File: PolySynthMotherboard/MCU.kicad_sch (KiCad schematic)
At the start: 21 parts, among them U201 STM32F411RETx, U202 74HC595, U203 74HC595, Y201 16MHz, Y202 32.768kHZ

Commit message: power supply/ output circuits
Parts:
- added C216, C217: 100n, Capacitor_SMD:C_0805_2012Metric, symbol Device:C
- added D201: 1N4148, Diode_THT:D_DO-35_SOD27_P7.62mm_Horizontal, symbol Diode:1N4148
- added D503: PMEG3030, PCM_Diode_SMD_AKL:D_SOD-123, symbol Device:D_Schottky
- added J201: SWD Header, Connector_PinHeader_1.27mm:PinHeader_2x07_P1.27mm_Horizontal, symbol Connector:ST_SWDHeader_3Wire
- added J202: USB_C_Receptacle_USB2.0, Connector_USB:USB_C_Receptacle_JAE_DX07S016JA1R1500, symbol Connector:USB_C_Receptacle_USB2.0
- added J203: MIDI_In, Connector_PinSocket_2.54mm:PinSocket_1x02_P2.54mm_Vertical, symbol Connector:Conn_01x02_Pin
- added J204: MIDI_Thru, Connector_PinSocket_2.54mm:PinSocket_1x02_P2.54mm_Vertical, symbol Connector:Conn_01x02_Pin
- added J205: MIDI_Out, Connector_PinSocket_2.54mm:PinSocket_1x02_P2.54mm_Vertical, symbol Connector:Conn_01x02_Pin
- added J401: Micro_SD_Card_Det2, Connector_Card:microSD_HC_Hirose_DM3D-SF, symbol Connector:Micro_SD_Card_Det2
- added R201, R202: 100k, PCM_Resistor_SMD_AKL:R_0805_2012Metric, symbol Device:R_US
- added R203: 4k7, PCM_Resistor_SMD_AKL:R_0805_2012Metric, symbol Device:R_US
- added R204, R206, R207, R208, R209: 220, PCM_Resistor_SMD_AKL:R_0805_2012Metric, symbol Device:R_US
- added R205: 470, PCM_Resistor_SMD_AKL:R_0805_2012Metric, symbol Device:R_US
- added R404: 47k, PCM_Resistor_SMD_AKL:R_0805_2012Metric, symbol Device:R_US
- added SW201: RST, Button_Switch_SMD:SW_SPST_B3U-1000P, symbol Switch:SW_SPST
- added SW202: BOOT, Button_Switch_SMD:SW_SPST_B3U-1000P, symbol Switch:SW_SPST
- added U204: 4N35, Package_DIP:DIP-6_W7.62mm, symbol Isolator:4N35
- added U205: 74HC04, PCM_Package_SO_AKL:SOIC-14_3.9x8.7mm_P1.27mm, symbol 74xx:74HC04
- C201, C202, C203, C204, C205, C208, C209, C210, C214, C215: footprint (none) -> Capacitor_SMD:C_0805_2012Metric
- U202, U203: footprint (none) -> Package_SO:SOIC-16_3.9x9.9mm_P1.27mm
- Y202: footprint (none) -> Crystal:Crystal_SMD_SeikoEpson_MC306-4Pin_8.0x3.2mm
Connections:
- net +3.3V: now also C217.1, J201.2 (VCC), J401.4 (VDD), R201.1, R205.1, R207.1, R209.1, R404.1, SW202.2 (B), U205.14 (VCC)
- net BOOT0: now also R202.1, SW202.1 (A)
- net DAC_A0: now also U201.27 (PB1); no longer U201.42 (PA9)
- net DAC_A1: now also U201.28 (PB2); no longer U201.43 (PA10)
- net DAC_A2: now also U201.29 (PB10); no longer U201.44 (PA11)
- net EXP_CS: now also U201.33 (PB12); no longer U201.50 (PA15)
- net EXP_MISO: now also U201.35 (PB14); no longer U201.52 (PC11)
- net EXP_MOSI: now also U201.36 (PB15); no longer U201.53 (PC12)
- net EXP_SCK: now also U201.34 (PB13); no longer U201.51 (PC10)
- net GND: now also C216.2, C217.2, J201.1 (GND), J202.A1 (GND), J202.A12 (GND), J202.B1 (GND), J202.B12 (GND), J202.S1 (SHIELD), J401.11 (SHIELD), J401.6 (VSS), R202.2, R203.2, SW201.1 (A), U204.4, U205.7 (GND)
- net NRST: now also C216.1, J201.6 (RST), R201.2, SW201.2 (B)
- net PITCH_MOSI: now also U201.23 (PA7)
- net PITCH_SCK: now also U201.21 (PA5)
- net POTS_SCL: now also U201.61 (PB8); no longer U201.58 (PB6)
- net POTS_SDA: now also U201.62 (PB9); no longer U201.59 (PB7)
- net SWO: now also J201.5 (SWO)
- net TCK: now also J201.3 (SWCLK)
- net TMS: now also J201.4 (SWDIO)
- net PIXELS_MAIN: now reaches U201.15 (PA1)
- net EXP_INTR_A: now reaches U201.37 (PC6)
- net EXP_INTR_B: now reaches U201.38 (PC7)
- net USB_D+: now reaches U201.45 (PA12)
- net USB_D+: now also J202.A6 (D+), J202.B6 (D+)
- net SD_CS: now reaches U201.54 (PD2)
- net SD_CS: now also J401.2 (DAT3/CD), R404.2
- net DISP_DC: now reaches U201.56 (PB4)
- net DISP_RST: now reaches U201.57 (PB5)
- net BATT_REF: now reaches U201.9 (PC1)
- net USART_RX: no longer names the net of U201.17 (PA3)
- net USART_TX renamed PIXELS_MATRIX
- new net: J204.2 (Pin_2), R207.2
- new net: D201.1 (K), J203.2 (Pin_2), U204.1
- new net: D201.2 (A), R204.1, U204.2
- new net: J202.A5 (CC1), J202.B5 (CC2), R203.1
- new net: U205.2, U205.3
- new net: R206.2, U205.4
- new net: J204.1 (Pin_1), R206.1
- new net: J205.2 (Pin_2), R209.2
- new net: J203.1 (Pin_1), R204.2
- new net: J205.1 (Pin_1), R208.1
- new net: R208.2, U205.8
- new net: U205.6, U205.9
- new net DISP_CS: U201.50 (PA15)
- new net DISP_MISO: J401.7 (DAT0), U201.52 (PC11)
- new net DISP_MOSI: J401.3 (CMD), U201.53 (PC12)
- new net DISP_SCK: J401.5 (CLK), U201.51 (PC10)
- new net EXP_INTR_C: U201.42 (PA9)
- new net MIDI_RX: R205.2, U201.59 (PB7), U204.5, U205.1
- new net MIDI_TX: U201.58 (PB6), U205.5
- new net USB_D-: J202.A7 (D-), J202.B7 (D-), U201.44 (PA11)
- new net VBUS: D503.2 (A), J202.A4 (VBUS), J202.A9 (VBUS), J202.B4 (VBUS), J202.B9 (VBUS)
- new net VDD: D503.1 (K)
- no-connect marks 5 -> 27
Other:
- note added: "Debug Header"
- note added: "MCU- STM32F411RETx"
- note added: "MIDI I/O"
- note added: "MicroSD reader"
- note added: "This SD card shares its SPI bus with the display"
- note added: "USB C Connector"
- moved on the sheet: C201, C202, C203, C204, C205, C206, C207, C208, C209, C210, C211, C212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

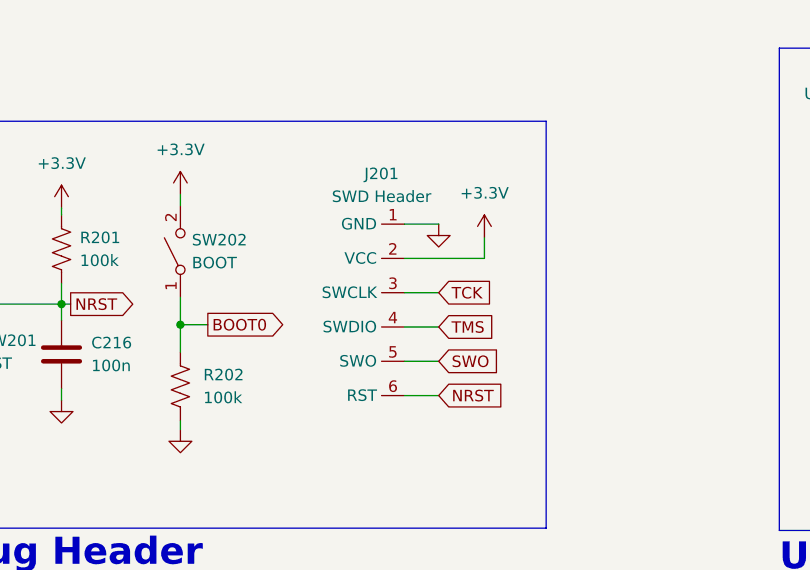
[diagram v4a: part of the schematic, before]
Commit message: net class assignment
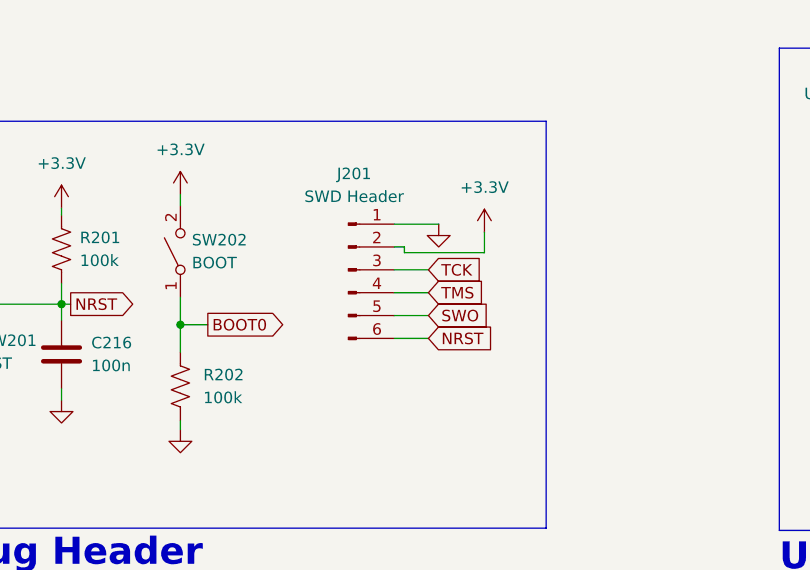
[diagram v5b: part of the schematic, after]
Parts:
- removed J201: SWD Header, Connector_PinHeader_1.27mm:PinHeader_2x07_P1.27mm_Horizontal, symbol Connector:ST_SWDHeader_3Wire
- added J201: SWD Header, Connector_PinHeader_2.54mm:PinHeader_1x06_P2.54mm_Vertical, symbol Connector:Conn_01x06_Pin
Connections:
- net +3.3V: now also J201.2 (Pin_2)
- net GND: now also J201.1 (Pin_1)
- net NRST: now also J201.6 (Pin_6)
- net SWO: now also J201.5 (Pin_5)
- net TCK: now also J201.3 (Pin_3)
- net TMS: now also J201.4 (Pin_4)
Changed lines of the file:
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@@
     (stroke (width 0) (type default))
   )
+  (wire (pts (xy 114.554 194.818) (xy 114.554 195.453))
+    (stroke (width 0) (type default))
+  )
   (wire (pts (xy 34.29 109.474) (xy 34.29 121.92))
     (stroke (width 0) (type default))
@@
     (stroke (width 0) (type default))
   )
-  (wire (pts (xy 114.554 199.898) (xy 118.364 199.898))
+  (wire (pts (xy 113.411 197.358) (xy 117.221 197.358))
     (stroke (width 0) (type default))
   )
@@
     (stroke (width 0) (type default))
   )
-  (wire (pts (xy 114.554 196.088) (xy 123.444 196.088))
+  (wire (pts (xy 114.554 195.453) (xy 123.444 195.453))
     (stroke (width 0) (type default))
   )
@@
     (stroke (width 0) (type default))
   )
+  (wire (pts (xy 113.411 194.818) (xy 114.554 194.818))
+    (stroke (width 0) (type default))
+  )
   (wire (pts (xy 200.914 81.026) (xy 204.724 81.026))
     (stroke (width 0) (type default))
@@
     (stroke (width 0) (type default))
   )
-  (wire (pts (xy 114.554 203.708) (xy 118.364 203.708))
+  (wire (pts (xy 113.411 199.898) (xy 117.221 199.898))
     (stroke (width 0) (type default))
   )
@@
     (stroke (width 0) (type default))
   )
-  (wire (pts (xy 123.444 196.088) (xy 123.444 193.802))
+  (wire (pts (xy 123.444 195.453) (xy 123.444 193.167))
     (stroke (width 0) (type default))
   )
@@
     (stroke (width 0) (type default))
   )
-  (wire (pts (xy 114.554 192.278) (xy 118.364 192.278))
-    (stroke (width 0) (type default))
-  )
   (wire (pts (xy 190.754 55.118) (xy 190.754 56.388))
     (stroke (width 0) (type default))
@@
     (stroke (width 0) (type default))
   )
-  (wire (pts (xy 114.554 211.328) (xy 118.364 211.328))
+  (wire (pts (xy 113.411 204.978) (xy 117.221 204.978))
     (stroke (width 0) (type default))
   )
@@
     (stroke (width 0) (type default))
   )
-  (wire (pts (xy 114.554 207.518) (xy 118.364 207.518))
+  (wire (pts (xy 113.411 202.438) (xy 117.221 202.438))
     (stroke (width 0) (type default))
   )
@@
     (stroke (width 0) (type default))
   )
+  (wire (pts (xy 113.411 192.278) (xy 118.364 192.278))
+    (stroke (width 0) (type default))
+  )
   (wire (pts (xy 279.654 50.419) (xy 286.639 50.419))
     (stroke (width 0) (type default))
@@
     )
   )
-  (global_label "SWO" (shape input) (at 118.364 207.518 0) (fields_autoplaced)
+  (global_label "SWO" (shape input) (at 117.221 202.438 0) (fields_autoplaced)
     (effects (font (size 1.27 1.27)) (justify left))
-    (property "Intersheetrefs" "${INTERSHEET_REFS}" (at 125.3406 207.518 0)
+    (property "Intersheetrefs" "${INTERSHEET_REFS}" (at 124.1976 202.438 0)
       (effects (font (size 1.27 1.27)) (justify left) hide)
     )
@@
     )
   )
-  (global_label "TCK" (shape input) (at 118.364 199.898 0) (fields_autoplaced)
+  (global_label "TCK" (shape input) (at 117.221 197.358 0) (fields_autoplaced)
     (effects (font (size 1.27 1.27)) (justify left))
-    (property "Intersheetrefs" "${INTERSHEET_REFS}" (at 124.8568 199.898 0)
+    (property "Intersheetrefs" "${INTERSHEET_REFS}" (at 123.7138 197.358 0)
       (effects (font (size 1.27 1.27)) (justify left) hide)
     )
@@
     )
   )
-  (global_label "TMS" (shape input) (at 118.364 203.708 0) (fields_autoplaced)
+  (global_label "TMS" (shape input) (at 117.221 199.898 0) (fields_autoplaced)
     (effects (font (size 1.27 1.27)) (justify left))
-    (property "Intersheetrefs" "${INTERSHEET_REFS}" (at 124.9777 203.708 0)
+    (property "Intersheetrefs" "${INTERSHEET_REFS}" (at 123.8347 199.898 0)
       (effects (font (size 1.27 1.27)) (justify left) hide)
     )
@@
     )
   )
-  (global_label "NRST" (shape input) (at 118.364 211.328 0) (fields_autoplaced)
+  (global_label "NRST" (shape input) (at 117.221 204.978 0) (fields_autoplaced)
     (effects (font (size 1.27 1.27)) (justify left))
-    (property "Intersheetrefs" "${INTERSHEET_REFS}" (at 126.1268 211.328 0)
+    (property "Intersheetrefs" "${INTERSHEET_REFS}" (at 124.9838 204.978 0)
       (effects (font (size 1.27 1.27)) (justify left) hide)
     )
@@
     )
   )
-  (symbol (lib_id "Connector:ST_SWDHeader_3Wire") (at 112.014 215.138 0) (unit 1)
-    (in_bom yes) (on_board yes) (dnp no)
-    (property "Reference" "J201" (at 112.014 186.69 0)
-      (effects (font (size 1.27 1.27)))
-    )
-    (property "Value" "SWD Header" (at 112.014 189.23 0)
-      (effects (font (size 1.27 1.27)))
-    )
-    (property "Footprint" "Connector_PinHeader_1.27mm:PinHeader_2x07_P1.27mm_Horizontal" (at 112.014 206.248 0)
-      (effects (font (size 1.27 1.27)) hide)
-    )
-    (property "Datasheet" "" (at 112.014 206.248 0)
-      (effects (font (size 1.27 1.27)) hide)
-    )
-    (pin "1")
-    (pin "2")
-    (pin "3")
-    (pin "4")
-    (pin "5")
-    (pin "6")
-    (instances
-      (project "PolySynthMotherboard"
-        (path "/22649217-9810-470f-bc7b-6f743ad2b90e/30ed774f-a7f6-4caf-bf27-d83abb3db248"
-          (reference "J201") (unit 1)
-        )
-      )
-    )
-  )
   (symbol (lib_id "Device:C") (at 83.566 119.38 0) (unit 1)
     (in_bom yes) (on_board yes) (dnp no)
@@
     )
   )
+  (symbol (lib_id "Connector:Conn_01x06_Pin") (at 108.331 197.358 0) (unit 1)
+    (in_bom yes) (on_board yes) (dnp no) (fields_autoplaced)
+    (property "Reference" "J201" (at 108.966 186.69 0)
+      (effects (font (size 1.27 1.27)))
+    )
+    (property "Value" "SWD Header" (at 108.966 189.23 0)
+      (effects (font (size 1.27 1.27)))
+    )
+    (property "Footprint" "Connector_PinHeader_2.54mm:PinHeader_1x06_P2.54mm_Vertical" (at 108.331 197.358 0)
+      (effects (font (size 1.27 1.27)) hide)
+    )
+    (property "Datasheet" "~" (at 108.331 197.358 0)
+      (effects (font (size 1.27 1.27)) hide)
+    )
+    (pin "1")
+    (pin "2")
+    (pin "3")
+    (pin "4")
+    (pin "5")
+    (pin "6")
+    (instances
+      (project "PolySynthMotherboard"
+        (path "/22649217-9810-470f-bc7b-6f743ad2b90e/30ed774f-a7f6-4caf-bf27-d83abb3db248"
+          (reference "J201") (unit 1)
+        )
+      )
+    )
+  )
   (symbol (lib_id "Connector:Conn_01x02_Pin") (at 391.795 113.792 180) (unit 1)
     (in_bom yes) (on_board yes) (dnp no)
@@
     )
   )
-  (symbol (lib_id "power:+3.3V") (at 123.444 193.802 0) (unit 1)
+  (symbol (lib_id "power:+3.3V") (at 123.444 193.167 0) (unit 1)
     (in_bom yes) (on_board yes) (dnp no) (fields_autoplaced)
-    (property "Reference" "#PWR0240" (at 123.444 197.612 0)
+    (property "Reference" "#PWR0240" (at 123.444 196.977 0)
       (effects (font (size 1.27 1.27)) hide)
     )
-    (property "Value" "+3.3V" (at 123.444 188.849 0)
+    (property "Value" "+3.3V" (at 123.444 188.214 0)
       (effects (font (size 1.27 1.27)))
     )
-    (property "Footprint" "" (at 123.444 193.802 0)
+    (property "Footprint" "" (at 123.444 193.167 0)
       (effects (font (size 1.27 1.27)) hide)
     )
-    (property "Datasheet" "" (at 123.444 193.802 0)
+    (property "Datasheet" "" (at 123.444 193.167 0)
       (effects (font (size 1.27 1.27)) hide)
     )
